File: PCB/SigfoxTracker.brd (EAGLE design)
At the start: 36.8 x 54.3 mm, 41 parts, among them IC1 WSSFM10R1AT, J1 SMA-J-P-H-ST-EM1, Q7 IRLML5203, U1 SIM28ML

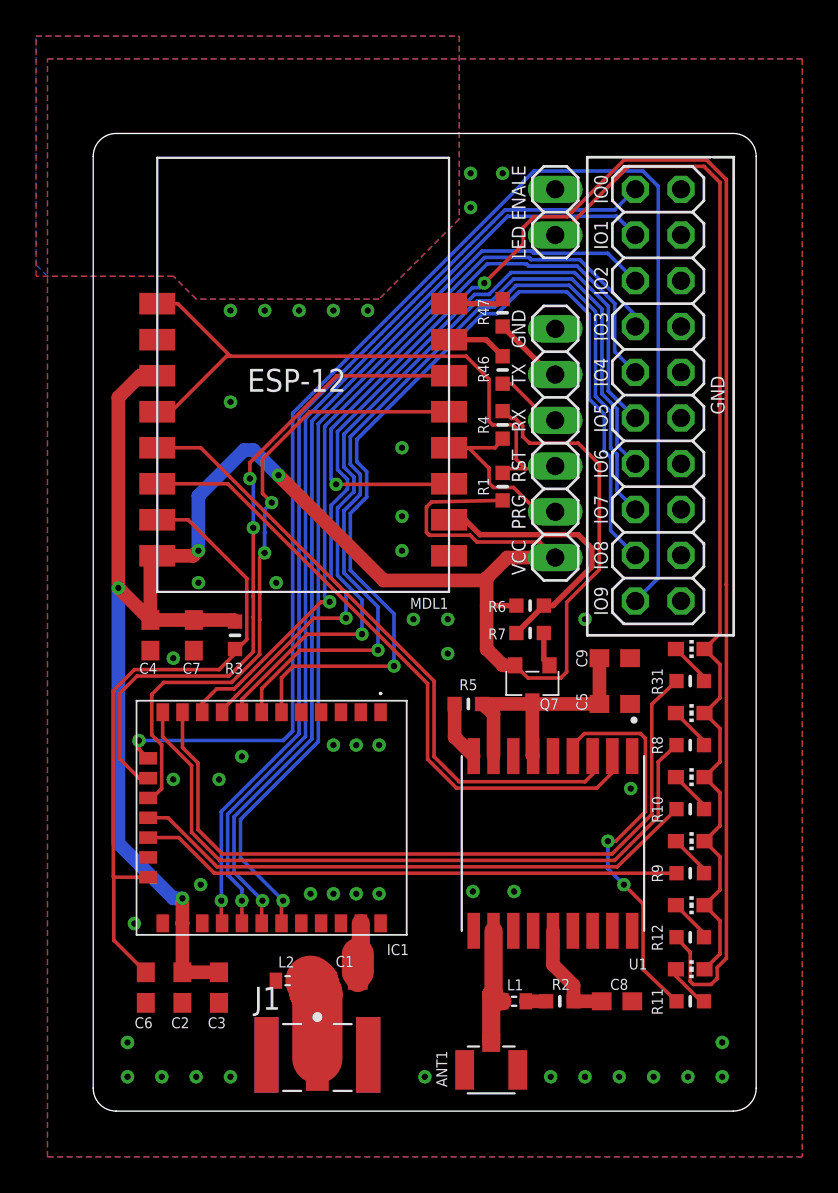
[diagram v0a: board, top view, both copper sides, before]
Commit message: More stitching, cleaned up schematic
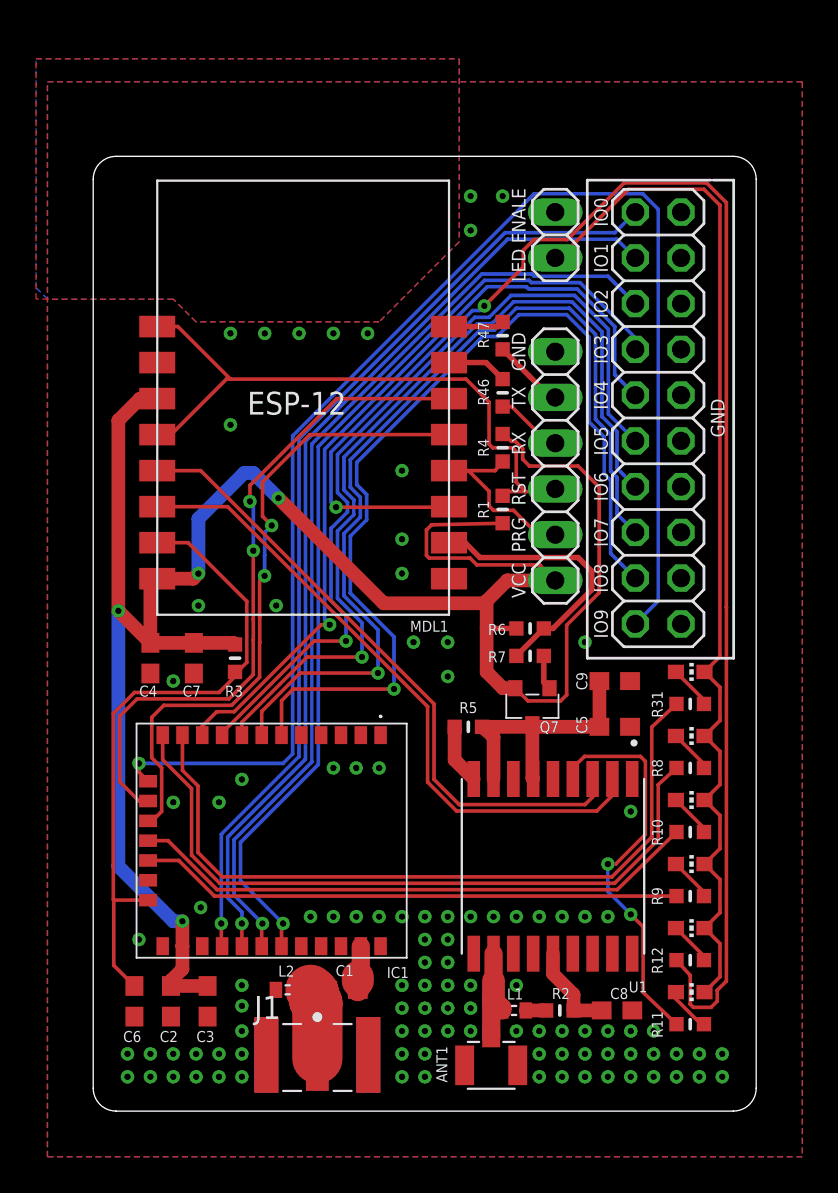
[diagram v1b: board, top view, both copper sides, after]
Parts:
- moved C5 1.27 mm to (29.0, 21.3)
- moved ENABLE_LED_JUMPER 1.27 mm to (25.7, 48.6)
- moved PROG 1.27 mm to (25.7, 35.8)
- moved R4 1.27 mm to (22.7, 36.8)
- moved R46 1.27 mm to (22.7, 39.9)
- moved R47 1.27 mm to (22.7, 43.1)
- moved R5 1.27 mm to (20.8, 21.3)
- moved SIGFOX_RX 1.27 mm to (33.1, 17.3)
- moved IC1 1.27 mm to (9.91, 15.2)
- moved SIGFOX_TX 1.27 mm to (33.1, 13.7)
- moved R11 1.27 mm to (33.1, 4.83)
- moved ACT 1.27 mm to (33.1, 10.2)
- moved C4 1.27 mm to (3.17, 25.1)
- moved C7 1.27 mm to (5.59, 25.1)
- moved C9 1.27 mm to (29.0, 23.9)
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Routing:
- net RF_IN: track 7.03 -> 5.57 mm
- net /SIGFOX_RST: track 36.8 -> 36.0 mm
- net SIGFOX_RF_IO: track 3.25 -> 2.49 mm
- net VCC_RF: track 5.95 -> 5.19 mm
- net N$2: track 6.73 -> 6.23 mm
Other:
- board size 36.8 x 54.3 mm -> 36.8 x 53 mm

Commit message: New revision, broken out i2C, ADC input, changed silkscreen
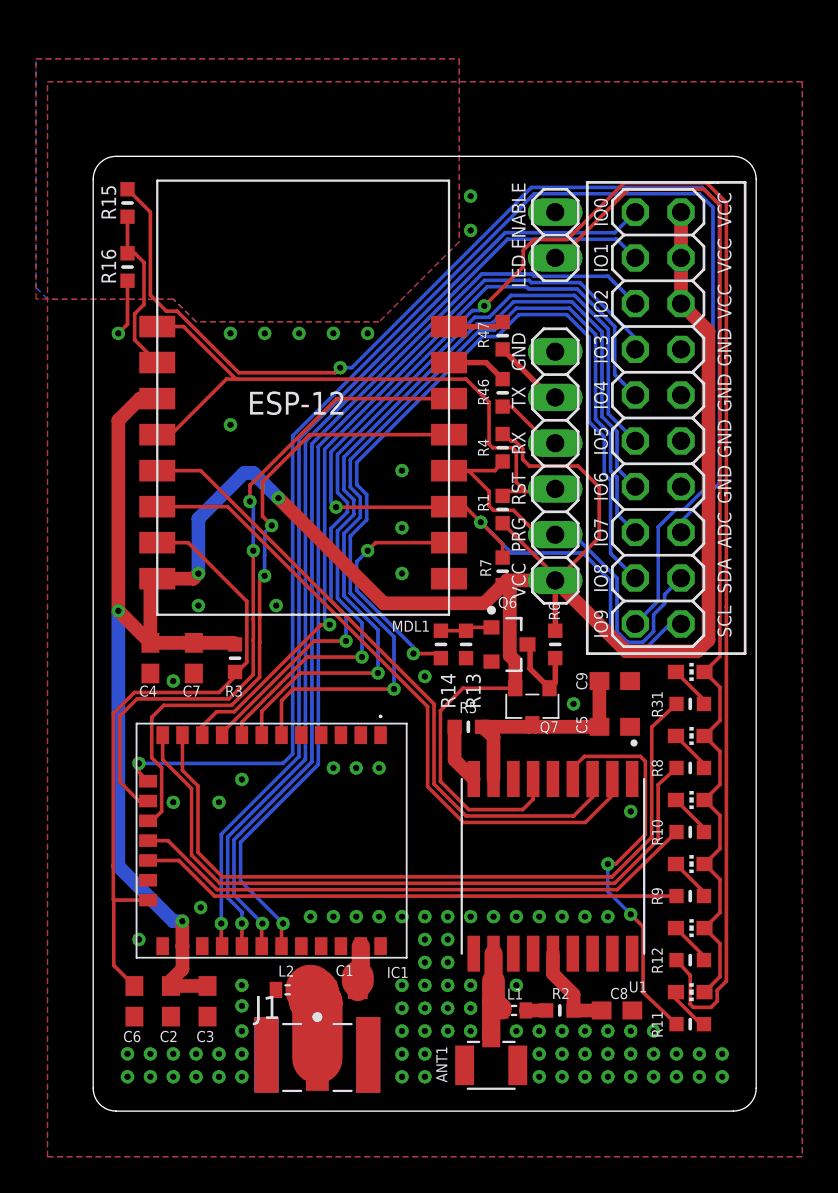
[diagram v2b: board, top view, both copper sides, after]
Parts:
- added Q6: ON_SEMICONDUCTOR_BC849BLT1GON_SEMICONDUCTOR_BC849BLT1G_0_0, On Semiconductor - BC849BLT1G:ON_SEMICONDUCTOR_BC849BLT1G_0
- added R13: 100k, ESP32_DMX_Audio:52101-101-REV-A_RC-MASTER-SMD_R0603MP
- added R14: 1K, ESP32_DMX_Audio:52101-101-REV-A_RC-MASTER-SMD_R0603MP
- added R15: 10K, ESP32_DMX_Audio:52101-101-REV-A_RC-MASTER-SMD_R0603MP
- added R16: 3V3, ESP32_DMX_Audio:52101-101-REV-A_RC-MASTER-SMD_R0603MP
- R4: value 100k -> 4K7
- R7: value 10R -> 4K7; device 52101-101-REV-A:RC-MASTER-SMD_R0603MP -> ESP32_DMX_Audio:52101-101-REV-A_RC-MASTER-SMD_R0603MP
- moved R7 4.94 mm to (22.7, 30.0), turned to 270 degrees
- moved R6 1.66 mm to (25.7, 25.9), turned to 90 degrees
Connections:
- removed net MCU_ACT: MDL1.11, R12.1
- removed net MOS_GATE: Q7.1, R7.1
- new net ADC_1V1: MDL1.2, R15.1, R16.2
- new net ADC_IN: JP1.16, R15.2
- new net ENABLE_GPS: MDL1.10, R14.2
- new net I2C_SCK: JP1.20, MDL1.11, R12.1, R7.1
- new net N$10: Q6.1, R13.2, R14.1
- net /ENABLE_GPS: now also Q6.3, Q7.1; no longer MDL1.10, R7.2
- net /PROG: now also JP1.18
- net GND: now also Q6.2, R13.1, R16.1; no longer JP1.16, JP1.18, JP1.2, JP1.20, JP1.4, JP1.6
- net GPS_VCC: no longer U1.6
- net VCC: now also JP1.2, JP1.4, JP1.6, R7.2, U1.6
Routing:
- net I2C_SCK: track 0.00 -> 108.5 mm, vias 0 -> 3
- net MCU_ACT: track 87.6 -> 0.00 mm, vias 2 -> 0
- net ADC_IN: track 0.00 -> 63.5 mm, vias 0 -> 1
- net VCC: track 122.5 -> 156.2 mm
- net ENABLE_GPS: track 0.00 -> 13.6 mm, vias 0 -> 2
- net /PROG: track 11.1 -> 24.6 mm
- net /ENABLE_GPS: track 15.3 -> 4.73 mm
- net ADC_1V1: track 0.00 -> 9.45 mm
- net SGPIO9: track 77.4 -> 82.0 mm
- net GND: track 0.00 -> 3.13 mm, vias 103 -> 101
- net GPS_VCC: track 15.4 -> 12.4 mm
- net N$10: track 0.00 -> 2.89 mm
- net MOS_GATE: track 1.92 -> 0.00 mm
- net MCU_RX1: track 36.0 -> 36.7 mm
- net MCU_TX1: track 35.5 -> 36.2 mm
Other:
- board text added: "/PRG"
- board text added: "/RST"
- board text added: "ADC"
- board text added: "LED ENABLE"
- board text added: "Multi-tracker dev board Smashcat 05/09/2020"
- board text added: "SCL"
- board text added: "SDA"
- board text removed: "/PROG"
- board text removed: "/RESET"
- board text removed: "ESP_ACTIVITY"
- board text removed: "LED ENALE"
- board text removed: "Multi-tracker dev board Smashcat 25/08/2020"
